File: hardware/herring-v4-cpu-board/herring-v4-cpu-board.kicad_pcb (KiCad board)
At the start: 4 copper layers, 100 x 60 mm, 18 parts, among them J1 Conn_02x20_Odd_Even, J2 Conn_02x10_Odd_Even, U1 W65C02, U2 ATF16V8B, U3 AT28C64B, U4 AS6C62256, X1 CXO_DIP8

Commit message: CPU board schematic mostly done, started routing
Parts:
- added C10: C, Capacitor_THT:C_Disc_D5.0mm_W2.5mm_P5.00mm, F.Cu at (80.2, 80.6)
- added C11: C, Capacitor_THT:C_Disc_D5.0mm_W2.5mm_P5.00mm, F.Cu at (102.7, 74.8)
- added C12: C, Capacitor_THT:C_Disc_D5.0mm_W2.5mm_P5.00mm, F.Cu at (116.8, 74.8)
- added C6: C, Capacitor_THT:C_Disc_D5.0mm_W2.5mm_P5.00mm, F.Cu at (31.8, 80.8)
- added C7: C, Capacitor_THT:C_Disc_D5.0mm_W2.5mm_P5.00mm, F.Cu at (45.7, 80.8)
- added C8: C, Capacitor_THT:C_Disc_D5.0mm_W2.5mm_P5.00mm, F.Cu at (59.7, 80.8)
- added C9: C, Capacitor_THT:C_Disc_D5.0mm_W2.5mm_P5.00mm, F.Cu at (73.7, 80.8)
- added R6: R, Resistor_THT:R_Axial_DIN0207_L6.3mm_D2.5mm_P7.62mm_Horizontal, F.Cu at (-89.1, 121.5)
- added U10: AS6C4008-55PCN, Package_DIP:DIP-32_W15.24mm, F.Cu at (75.0, 25.0)
- added U11: ATF22V10C, Package_DIP:DIP-24_W7.62mm, F.Cu at (95.0, 78.0)
- added U5: 74HC245, Package_DIP:DIP-20_W7.62mm, F.Cu at (24.0, 84.0)
- added U6: 74HC245, Package_DIP:DIP-20_W7.62mm, F.Cu at (66.0, 84.0)
- added U8: W65C22, Package_DIP:DIP-40_W15.24mm, F.Cu at (50.0, 25.0)
- added U9: SST39SF040, Package_DIP:DIP-32_W15.24mm, F.Cu at (100.0, 25.0)
- C1: value C -> C_Polarized; footprint Capacitor_THT:C_Disc_D4.3mm_W1.9mm_P5.00mm -> Capacitor_THT:CP_Radial_D10.0mm_P3.80mm
- C2, C3, C4, C5: footprint Capacitor_THT:C_Disc_D4.3mm_W1.9mm_P5.00mm -> Capacitor_THT:C_Disc_D5.0mm_W2.5mm_P5.00mm
- U2: value ATF16V8B -> 74HC245
- U3: value AT28C64B -> ATF22V10C; footprint Package_DIP:DIP-28_W15.24mm -> Package_DIP:DIP-24_W7.62mm
- U4: value AS6C62256 -> 74HC245; footprint Package_DIP:DIP-28_W15.24mm -> Package_DIP:DIP-20_W7.62mm
- moved R5 209.9 mm to (-87.5, 112.5), turned to 0 degrees
- moved R4 209.7 mm to (-87.5, 108.4), turned to 0 degrees
- moved R3 196.1 mm to (-87.5, 104.3), turned to 0 degrees
- moved R2 196.0 mm to (-87.5, 100.3), turned to 0 degrees
- moved R1 194.4 mm to (-87.5, 96.2), turned to 0 degrees
- moved C1 96.5 mm to (82.6, 103.0)
- moved X1 65.3 mm to (80.6, 92.6)
- moved C2 63.5 mm to (22.0, 42.8), turned to -90 degrees
- moved U4 53.3 mm to (52.0, 84.0), turned to 0 degrees
- moved C4 47.3 mm to (90.2, 21.8), turned to 180 degrees
- moved C5 44.1 mm to (115.2, 21.8), turned to 180 degrees
- moved J1 40.0 mm to (25.0, 115.0)
- moved J2 40.0 mm to (90.0, 115.0)
- moved G*** 33.8 mm to (74.0, 69.8)
- moved C3 33.7 mm to (47.0, 73.2), turned to 90 degrees
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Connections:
- net //RES renamed /RES
- J1 pad 10: /D5 -> D5
- J1 pad 11: /D6 -> D6
- J1 pad 12: /D7 -> D7
- J1 pad 13: /A0 -> A0
- J1 pad 14: /A1 -> A1
- J1 pad 15: /A2 -> A2
- J1 pad 16: /A3 -> A3
- J1 pad 17: /A4 -> A4
- J1 pad 18: /A5 -> A5
- J1 pad 19: /A6 -> A6
- J1 pad 20: /A7 -> A7
- J1 pad 23: /A8 -> A8
- J1 pad 24: /A9 -> A9
- J1 pad 25: /A10 -> A10
- J1 pad 26: /A11 -> A11
- J1 pad 27: /A12 -> A12
- J1 pad 28: /A13 -> A13
- J1 pad 29: /A14 -> A14
- J1 pad 30: /A15 -> A15
- J1 pad 31: /CLK -> CLK
- J1 pad 32: //CS_IO -> /IRQEXP
- J1 pad 33: //RW -> /RW
- J1 pad 34: //WR -> /NMI
- J1 pad 35: //IRQ -> BE
- J1 pad 36: //NMI -> RDY
- J1 pad 5: /D0 -> D0
- J1 pad 6: /D1 -> D1
- J1 pad 7: /D2 -> D2
- J1 pad 8: /D3 -> D3
- J1 pad 9: /D4 -> D4
- J2 pad 10: unconnected-(J2-Pad10) -> SPI_CLK
- J2 pad 11: unconnected-(J2-Pad11) -> SPI_DI
- J2 pad 12: unconnected-(J2-Pad12) -> SPI_DO
- J2 pad 13: unconnected-(J2-Pad13) -> SPI_CS0
- J2 pad 14: unconnected-(J2-Pad14) -> SPI_CS1
- J2 pad 15: unconnected-(J2-Pad15) -> SPI_CS2
- J2 pad 16: unconnected-(J2-Pad16) -> SPI_CS3
- J2 pad 17: unconnected-(J2-Pad17) -> SPI_INT0
- J2 pad 18: unconnected-(J2-Pad18) -> SPI_INT1
- J2 pad 3: //ML -> /CS0
- J2 pad 4: /RDY -> /CS1
- J2 pad 5: /BE -> /CS2
- J2 pad 6: /SYNC -> /CS3
- J2 pad 7: //VP -> /CS4
- J2 pad 8: unconnected-(J2-Pad8) -> /CS5
- J2 pad 9: unconnected-(J2-Pad9) -> /CS6
- R2 pad 2: //NMI -> /NMI
- R3 pad 2: //IRQ -> /IRQ
- R4 pad 2: /BE -> BE
- R5 pad 2: /RDY -> Net-(U1-~{SO})
- U1 pad 1: //VP -> unconnected-(U1-~{VP}-Pad1)
- U1 pad 10: /A1 -> A1CPU
- U1 pad 11: /A2 -> A2CPU
- U1 pad 12: /A3 -> A3CPU
- U1 pad 13: /A4 -> A4CPU
- U1 pad 14: /A5 -> A5CPU
- U1 pad 15: /A6 -> A6CPU
- U1 pad 16: /A7 -> A7CPU
- U1 pad 17: /A8 -> A8CPU
- U1 pad 18: /A9 -> A9CPU
- U1 pad 19: /A10 -> A10CPU
- U1 pad 2: /RDY -> RDY
- U1 pad 20: /A11 -> A11CPU
- U1 pad 22: /A12 -> A12CPU
- U1 pad 23: /A13 -> A13CPU
- U1 pad 24: /A14 -> A14CPU
- U1 pad 25: /A15 -> A15CPU
- U1 pad 26: /D7 -> D7CPU
- U1 pad 27: /D6 -> D6CPU
- U1 pad 28: /D5 -> D5CPU
- U1 pad 29: /D4 -> D4CPU
- U1 pad 30: /D3 -> D3CPU
- U1 pad 31: /D2 -> D2CPU
- U1 pad 32: /D1 -> D1CPU
- U1 pad 33: /D0 -> D0CPU
- U1 pad 34: //RW -> /RWCPU
- U1 pad 36: /BE -> BE
- U1 pad 37: /CLK -> CLKCPU
- U1 pad 38: +5V -> Net-(U1-~{SO})
- U1 pad 4: //IRQ -> /IRQ
- U1 pad 5: //ML -> unconnected-(U1-~{ML}-Pad5)
- U1 pad 6: //NMI -> /NMI
- U1 pad 7: /SYNC -> unconnected-(U1-SYNC-Pad7)
- U1 pad 9: /A0 -> A0CPU
- U2 pad 1: /CLK -> GND
- U2 pad 11: //RW -> A0CPU
- U2 pad 12: //ROM0 -> A1CPU
- U2 pad 13: //RAM0 -> A2CPU
- U2 pad 14: //CS_IO -> A3CPU
- U2 pad 15: //WR -> A4CPU
- U2 pad 16: unconnected-(U2-Pad16) -> A5CPU
- U2 pad 17: unconnected-(U2-Pad17) -> A6CPU
- U2 pad 18: unconnected-(U2-Pad18) -> A7CPU
- U2 pad 19: unconnected-(U2-Pad19) -> /BUFFERS
- U2 pad 2: /A8 -> A7
- U2 pad 3: /A9 -> A6
- U2 pad 4: /A10 -> A5
- U2 pad 5: /A11 -> A4
- U2 pad 6: /A12 -> A3
- U2 pad 7: /A13 -> A2
- U2 pad 8: /A14 -> A1
- U2 pad 9: /A15 -> A0
- U3 pad 1: unconnected-(U3-Pad1) -> BE
- U3 pad 10: /A0 -> A14CPU
- U3 pad 11: /D0 -> A15CPU
- U3 pad 12: /D1 -> GND
- U3 pad 13: /D2 -> GND
- U3 pad 14: GND -> /BUFFERS
- U3 pad 15: /D3 -> unconnected-(U3-IO1-Pad15)
- U3 pad 16: /D4 -> /CSVIA
- U3 pad 17: /D5 -> /CS6
- U3 pad 18: /D6 -> /CS5
- U3 pad 19: /D7 -> /CS4
- U3 pad 2: /A12 -> A6CPU
- U3 pad 20: //ROM0 -> /CS3
- U3 pad 21: /A10 -> /CS2
- U3 pad 22: GND -> /CS1
- U3 pad 23: /A11 -> /CS0
- U3 pad 24: /A9 -> +5V
- U3 pad 3: /A7 -> A7CPU
- U3 pad 4: /A6 -> A8CPU
- U3 pad 5: /A5 -> A9CPU
- U3 pad 6: /A4 -> A10CPU
- U3 pad 7: /A3 -> A11CPU
- U3 pad 8: /A2 -> A12CPU
- U3 pad 9: /A1 -> A13CPU
- U4 pad 1: /A14 -> GND
- U4 pad 10: /A0 -> GND
- U4 pad 11: /D0 -> A8CPU
- U4 pad 12: /D1 -> A9CPU
- U4 pad 13: /D2 -> A10CPU
- U4 pad 14: GND -> A11CPU
- U4 pad 15: /D3 -> A12CPU
- U4 pad 16: /D4 -> A13CPU
- U4 pad 17: /D5 -> A14CPU
- U4 pad 18: /D6 -> A15CPU
- U4 pad 19: /D7 -> /BUFFERS
- U4 pad 2: /A12 -> A15
- U4 pad 20: //RAM0 -> +5V
- U4 pad 3: /A7 -> A14
- U4 pad 4: /A6 -> A13
- U4 pad 5: /A5 -> A12
- U4 pad 6: /A4 -> A11
- U4 pad 7: /A3 -> A10
- U4 pad 8: /A2 -> A9
- U4 pad 9: /A1 -> A8
- X1 pad 5: /CLK -> CLKCPU
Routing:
- net /D1: track 162.1 -> 0.00 mm, vias 1 -> 0
- net /D2: track 159.3 -> 0.00 mm, vias 1 -> 0
- net /D0: track 158.5 -> 0.00 mm, vias 1 -> 0
- net /D3: track 155.2 -> 0.00 mm, vias 1 -> 0
- net /D5: track 147.3 -> 0.00 mm, vias 1 -> 0
- net /D4: track 147.2 -> 0.00 mm, vias 1 -> 0
- net /D6: track 138.5 -> 0.00 mm, vias 1 -> 0
- net /D7: track 137.2 -> 0.00 mm, vias 1 -> 0
- net /RES: track 130.3 -> 0.00 mm, vias 2 -> 0
- net /RDY: track 126.6 -> 0.00 mm, vias 2 -> 0
- net /A0: track 121.8 -> 0.00 mm, vias 1 -> 0
- net //IRQ: track 121.4 -> 0.00 mm, vias 4 -> 0
- net /BE: track 121.2 -> 0.00 mm, vias 2 -> 0
- net /A1: track 119.2 -> 0.00 mm, vias 1 -> 0
- net /A2: track 111.2 -> 0.00 mm, vias 1 -> 0
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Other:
- board size 100 x 60 mm -> 100 x 100 mm
- board text added: "Herring v4 CPU Board Rev 1.0a github.com/crmaykish/herring-6502"
- board text removed: "32K SRAM"
- board text removed: "65C02"
- board text removed: "8K ROM"
- board text removed: "CLOCK"
- board text removed: "GAL16V8"
- board text removed: "Herring v4 Core Board Rev 1.0a Colin Maykish - 2024"
- board text removed: "JLCJLCJLCJLC"
- board text removed: "github.com/crmaykish/herring-6502"

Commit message: Routed buffers and expansion header
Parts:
- removed C1: C_Polarized, Capacitor_THT:CP_Radial_D10.0mm_P3.80mm
- removed C10, C11, C12: C, Capacitor_THT:C_Disc_D5.0mm_W2.5mm_P5.00mm
- removed the C4 at (90.2, 21.8)
- removed the C5 at (115.2, 21.8)
- removed the C6 at (31.8, 80.8)
- removed R1, R2, R3, R4, R5, R6: R, Resistor_THT:R_Axial_DIN0207_L6.3mm_D2.5mm_P7.62mm_Horizontal
- removed U1: W65C02, Package_DIP:DIP-40_W15.24mm
- removed U10: AS6C4008-55PCN, Package_DIP:DIP-32_W15.24mm
- removed U11: ATF22V10C, Package_DIP:DIP-24_W7.62mm
- removed the U3 at (109.0, 78.0)
- removed the U8 at (50.0, 25.0)
- removed U9: SST39SF040, Package_DIP:DIP-32_W15.24mm
- removed X1: CXO_DIP8, Oscillator:Oscillator_DIP-8
- added U2: ATF22V10C, Package_DIP:DIP-24_W7.62mm, F.Cu at (80.0, 78.9)
- moved G*** 105.2 mm to (178.5, 81.6)
- moved C3 44.5 mm to (45.7, 80.4), turned to 180 degrees
- moved C5 27.6 mm to (73.8, 80.0), turned to 180 degrees
- moved C6 14.9 mm to (87.3, 74.8)
- moved C2 14.0 mm to (31.7, 80.0)
- renumbered C7 to C2, C2 to C3, C8 to C4, C3 to C5, C9 to C6, U2 to U3, U5 to U6, U6 to U8
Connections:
- J1 pad 10: D5 -> BD5
- J1 pad 11: D6 -> BD6
- J1 pad 12: D7 -> BD7
- J1 pad 13: A0 -> BA0
- J1 pad 14: A1 -> BA1
- J1 pad 15: A2 -> BA2
- J1 pad 16: A3 -> BA3
- J1 pad 17: A4 -> BA4
- J1 pad 18: A5 -> BA5
- J1 pad 19: A6 -> BA6
- J1 pad 20: A7 -> BA7
- J1 pad 23: A8 -> BA8
- J1 pad 24: A9 -> BA9
- J1 pad 25: A10 -> BA10
- J1 pad 26: A11 -> BA11
- J1 pad 27: A12 -> BA12
- J1 pad 28: A13 -> BA13
- J1 pad 29: A14 -> BA14
- J1 pad 30: A15 -> BA15
- J1 pad 31: CLK -> BCLKCPU
- J1 pad 32: /IRQEXP -> /BRW
- J1 pad 33: /RW -> BE
- J1 pad 34: /NMI -> /MEMWR
- J1 pad 35: BE -> /IOREQ
- J1 pad 36: RDY -> /MEMRQ
- J1 pad 5: D0 -> BD0
- J1 pad 6: D1 -> BD1
- J1 pad 7: D2 -> BD2
- J1 pad 8: D3 -> BD3
- J1 pad 9: D4 -> BD4
- J2 pad 3: /CS0 -> /IRQ0
- J2 pad 4: /CS1 -> /IRQ1
- J2 pad 5: /CS2 -> /IRQ2
- J2 pad 6: /CS3 -> /IRQ3
- J2 pad 7: /CS4 -> /NMI
- J2 pad 8: /CS5 -> /BVP
- J2 pad 9: /CS6 -> RDY
- U3 pad 11: A0CPU -> A0
- U3 pad 12: A1CPU -> A1
- U3 pad 13: A2CPU -> A2
- U3 pad 14: A3CPU -> A3
- U3 pad 15: A4CPU -> A4
- U3 pad 16: A5CPU -> A5
- U3 pad 17: A6CPU -> A6
- U3 pad 18: A7CPU -> A7
- U3 pad 2: A7 -> BA7
- U3 pad 3: A6 -> BA6
- U3 pad 4: A5 -> BA5
- U3 pad 5: A4 -> BA4
- U3 pad 6: A3 -> BA3
- U3 pad 7: A2 -> BA2
- U3 pad 8: A1 -> BA1
- U3 pad 9: A0 -> BA0
- U4 pad 11: A8CPU -> A8
- U4 pad 12: A9CPU -> A9
- U4 pad 13: A10CPU -> A10
- U4 pad 14: A11CPU -> A11
- U4 pad 15: A12CPU -> A12
- U4 pad 16: A13CPU -> A13
- U4 pad 17: A14CPU -> A14
- U4 pad 18: A15CPU -> A15
- U4 pad 2: A15 -> BA15
- U4 pad 3: A14 -> BA14
- U4 pad 4: A13 -> BA13
- U4 pad 5: A12 -> BA12
- U4 pad 6: A11 -> BA11
- U4 pad 7: A10 -> BA10
- U4 pad 8: A9 -> BA9
- U4 pad 9: A8 -> BA8
- U6 pad 1: /RWCPU -> /RW
- U6 pad 11: D0CPU -> D0
- U6 pad 12: D1CPU -> D1
- U6 pad 13: D2CPU -> D2
- U6 pad 14: D3CPU -> D3
- U6 pad 15: D4CPU -> D4
- U6 pad 16: D5CPU -> D5
- U6 pad 17: D6CPU -> D6
- U6 pad 18: D7CPU -> D7
- U6 pad 2: D7 -> BD7
- U6 pad 3: D6 -> BD6
- U6 pad 4: D5 -> BD5
- U6 pad 5: D4 -> BD4
- U6 pad 6: D3 -> BD3
- U6 pad 7: D2 -> BD2
- U6 pad 8: D1 -> BD1
- U6 pad 9: D0 -> BD0
- U8 pad 1: +5V -> GND
- U8 pad 11: unconnected-(U6-B7-Pad11) -> GND
- U8 pad 12: unconnected-(U6-B6-Pad12) -> GND
- U8 pad 13: unconnected-(U6-B5-Pad13) -> GND
- U8 pad 14: unconnected-(U6-B4-Pad14) -> GND
- U8 pad 15: unconnected-(U6-B3-Pad15) -> GND
- U8 pad 16: unconnected-(U6-B2-Pad16) -> CLKCPU
- U8 pad 18: CLK -> /VP
- U8 pad 2: CLKCPU -> /BVP
- U8 pad 3: /RWCPU -> /BRW
- U8 pad 4: GND -> BCLKCPU
- U8 pad 5: GND -> unconnected-(U8-A3-Pad5)
- U8 pad 6: GND -> unconnected-(U8-A4-Pad6)
- U8 pad 7: GND -> unconnected-(U8-A5-Pad7)
- U8 pad 8: GND -> unconnected-(U8-A6-Pad8)
- U8 pad 9: GND -> unconnected-(U8-A7-Pad9)
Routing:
- net /BUFFERS: track 0.00 -> 79.1 mm, vias 0 -> 4
- net /RW: track 0.00 -> 67.6 mm, vias 0 -> 1
- net /BVP: track 0.00 -> 62.4 mm, vias 0 -> 2
- net /MEMWR: track 0.00 -> 48.8 mm, vias 0 -> 2
- net BE: track 0.00 -> 47.5 mm, vias 0 -> 2
- net /MEMRQ: track 0.00 -> 43.1 mm, vias 0 -> 2
- net /IOREQ: track 0.00 -> 42.9 mm, vias 0 -> 2
- net D7: track 39.0 -> 0.00 mm
- net BD7: track 0.00 -> 39.0 mm
- net BA7: track 0.00 -> 36.4 mm
- net A7: track 36.4 -> 0.00 mm
- net BA15: track 0.00 -> 35.6 mm
- net D6: track 32.8 -> 0.00 mm
- net BD6: track 0.00 -> 32.8 mm
- net D5: track 32.5 -> 0.00 mm
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
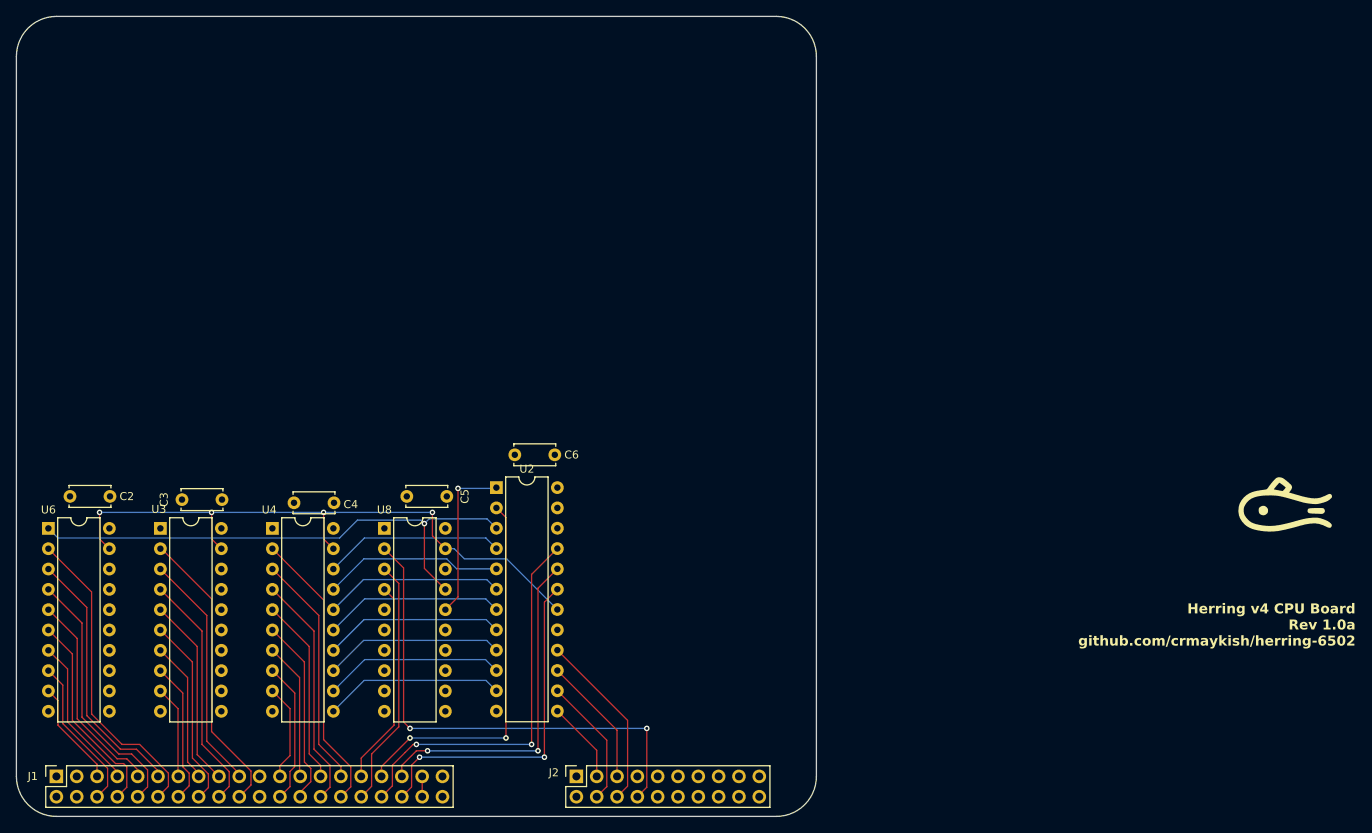
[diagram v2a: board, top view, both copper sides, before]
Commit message: v4 CPU board fully routed, needs cleanup
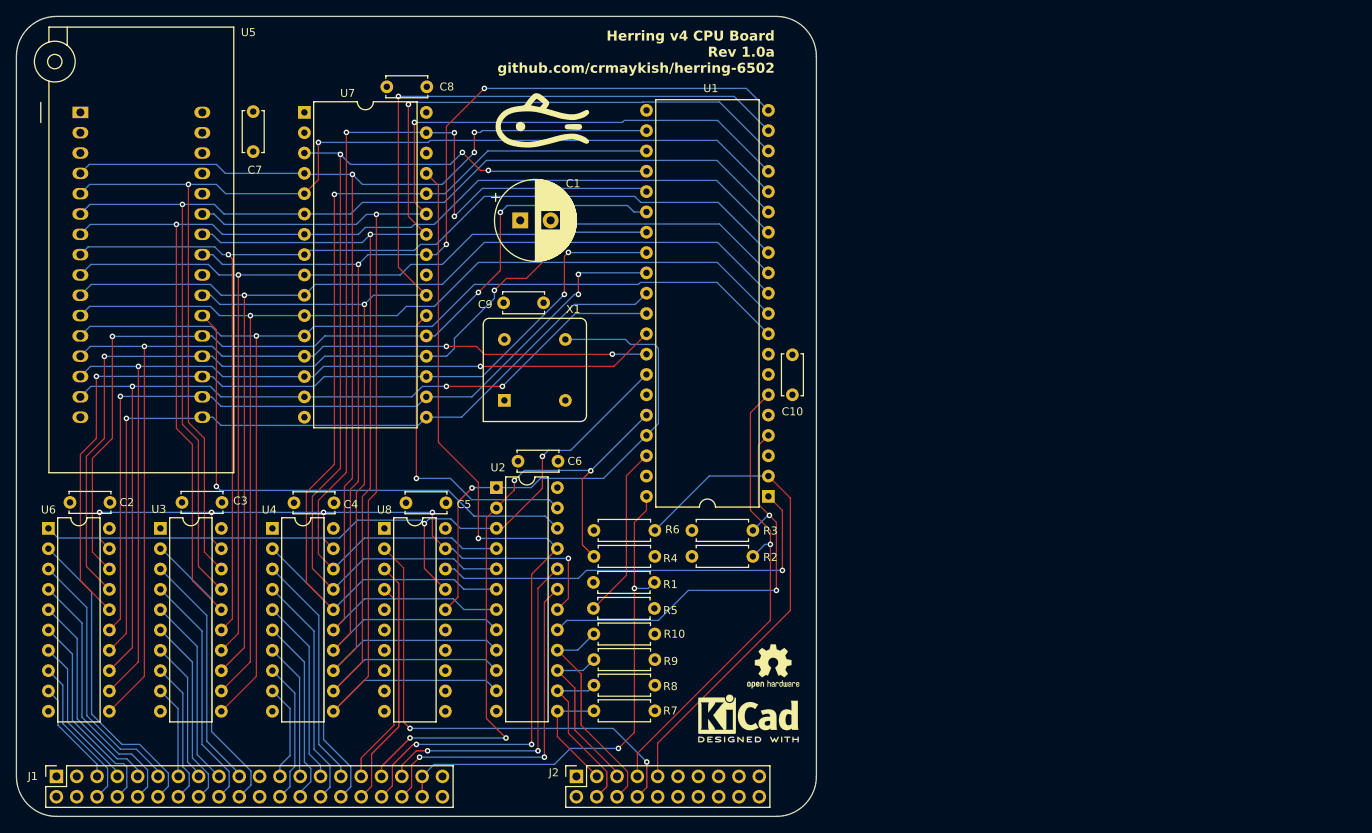
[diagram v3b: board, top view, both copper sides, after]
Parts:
- added C1: C_Polarized, Capacitor_THT:CP_Radial_D10.0mm_P3.80mm, F.Cu at (83.0, 45.5)
- added C10: C, Capacitor_THT:C_Disc_D5.0mm_W2.5mm_P5.00mm, F.Cu at (117.0, 62.3)
- added C7: C, Capacitor_THT:C_Disc_D5.0mm_W2.5mm_P5.00mm, F.Cu at (49.6, 31.9)
- added C8: C, Capacitor_THT:C_Disc_D5.0mm_W2.5mm_P5.00mm, F.Cu at (71.3, 28.8)
- added C9: C, Capacitor_THT:C_Disc_D5.0mm_W2.5mm_P5.00mm, F.Cu at (80.9, 55.8)
- added R1: R, Resistor_THT:R_Axial_DIN0207_L6.3mm_D2.5mm_P7.62mm_Horizontal, F.Cu at (92.1, 90.8)
- added R10: R, Resistor_THT:R_Axial_DIN0207_L6.3mm_D2.5mm_P7.62mm_Horizontal, F.Cu at (92.2, 97.2)
- added R2: R, Resistor_THT:R_Axial_DIN0207_L6.3mm_D2.5mm_P7.62mm_Horizontal, F.Cu at (104.4, 87.5)
- added R3: R, Resistor_THT:R_Axial_DIN0207_L6.3mm_D2.5mm_P7.62mm_Horizontal, F.Cu at (104.4, 84.2)
- added R4: R, Resistor_THT:R_Axial_DIN0207_L6.3mm_D2.5mm_P7.62mm_Horizontal, F.Cu at (99.8, 87.5)
- added R5: R, Resistor_THT:R_Axial_DIN0207_L6.3mm_D2.5mm_P7.62mm_Horizontal, F.Cu at (99.8, 94.0)
- added R6: R, Resistor_THT:R_Axial_DIN0207_L6.3mm_D2.5mm_P7.62mm_Horizontal, F.Cu at (92.2, 84.2)
- added R7: R, Resistor_THT:R_Axial_DIN0207_L6.3mm_D2.5mm_P7.62mm_Horizontal, F.Cu at (92.2, 106.8)
- added R8: R, Resistor_THT:R_Axial_DIN0207_L6.3mm_D2.5mm_P7.62mm_Horizontal, F.Cu at (92.2, 103.6)
- added R9: R, Resistor_THT:R_Axial_DIN0207_L6.3mm_D2.5mm_P7.62mm_Horizontal, F.Cu at (92.2, 100.4)
- added REF**: KiCad-Logo2_5mm_SilkScreen, Symbol:KiCad-Logo2_5mm_SilkScreen, F.Cu at (111.5, 107.8)
- added REF**: OSHW-Logo2_7.3x6mm_SilkScreen, Symbol:OSHW-Logo2_7.3x6mm_SilkScreen, F.Cu at (114.6, 101.2)
- added U1: W65C02, Package_DIP:DIP-40_W15.24mm, F.Cu at (114.0, 80.0)
- added U5: SST39SF040, Socket:DIP_Socket-32_W11.9_W12.7_W15.24_W17.78_W18.5_3M_232-1285-00-0602J, F.Cu at (28.0, 32.0)
- added U7: AS6C4008-55PCN, Package_DIP:DIP-32_W15.24mm, F.Cu at (56.0, 32.0)
- added X1: CXO_DIP8, Oscillator:Oscillator_DIP-8, F.Cu at (81.0, 68.0)
- moved G*** 104.5 mm to (85.7, 33.6)
- moved C6 0.89 mm to (87.7, 75.6)
- moved C5 0.81 mm to (73.7, 80.8)
- moved C2 0.75 mm to (31.7, 80.8)
- moved C3 0.35 mm to (45.7, 80.8)
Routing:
- net A9: track 22.6 -> 175.2 mm, vias 0 -> 2
- net A8: track 22.5 -> 175.0 mm, vias 0 -> 2
- net A10: track 22.5 -> 173.1 mm, vias 0 -> 2
- net A7: track 0.00 -> 144.9 mm, vias 0 -> 2
- net A5: track 0.00 -> 143.0 mm, vias 0 -> 1
- net A6: track 0.00 -> 142.6 mm, vias 0 -> 1
- net A0: track 0.00 -> 141.2 mm, vias 0 -> 1
- net A1: track 0.00 -> 140.8 mm, vias 0 -> 1
- net A2: track 0.00 -> 140.6 mm, vias 0 -> 1
- net A4: track 0.00 -> 140.4 mm, vias 0 -> 1
- net A3: track 0.00 -> 140.1 mm, vias 0 -> 1
- net A11: track 22.5 -> 162.2 mm, vias 0 -> 3
- net A12: track 22.6 -> 157.0 mm, vias 0 -> 3
- net D0: track 0.00 -> 120.1 mm, vias 0 -> 3
- net D1: track 0.00 -> 116.1 mm, vias 0 -> 2
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
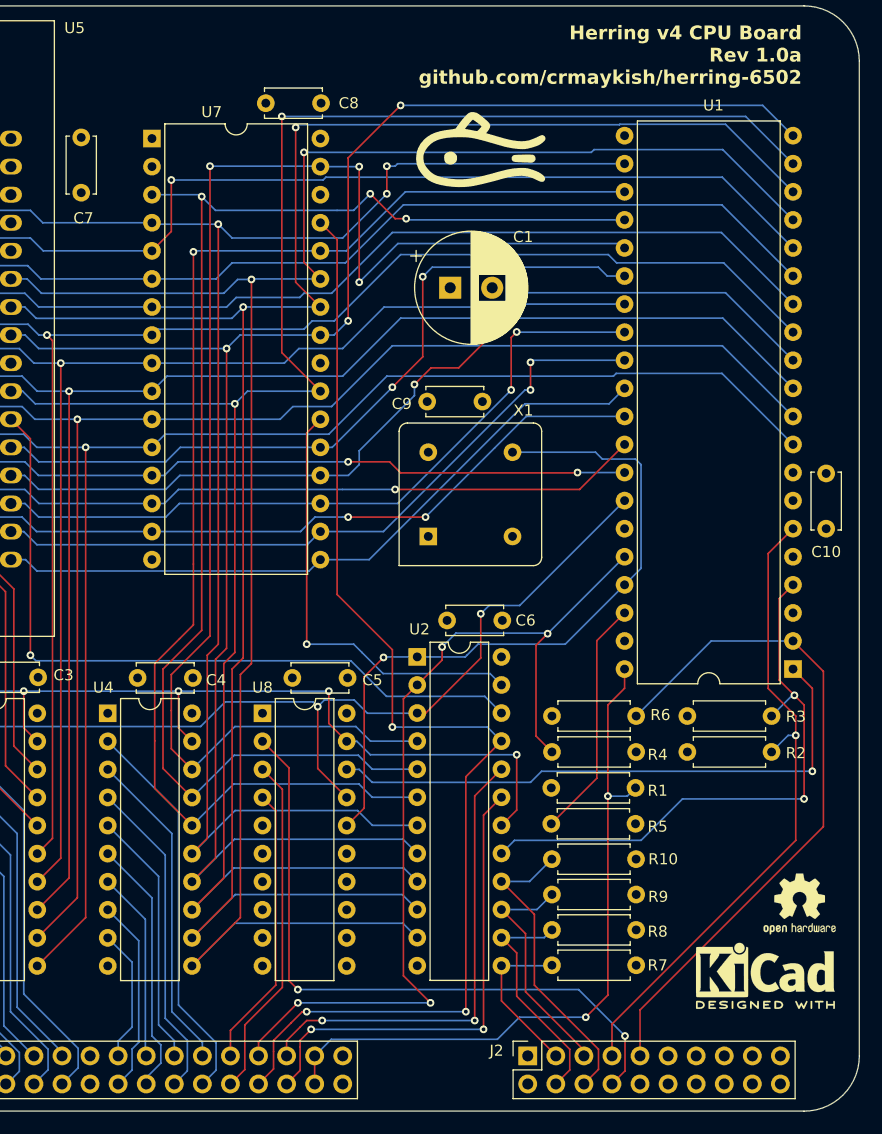
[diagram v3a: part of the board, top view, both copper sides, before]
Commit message: Stub out v4 ACIA board
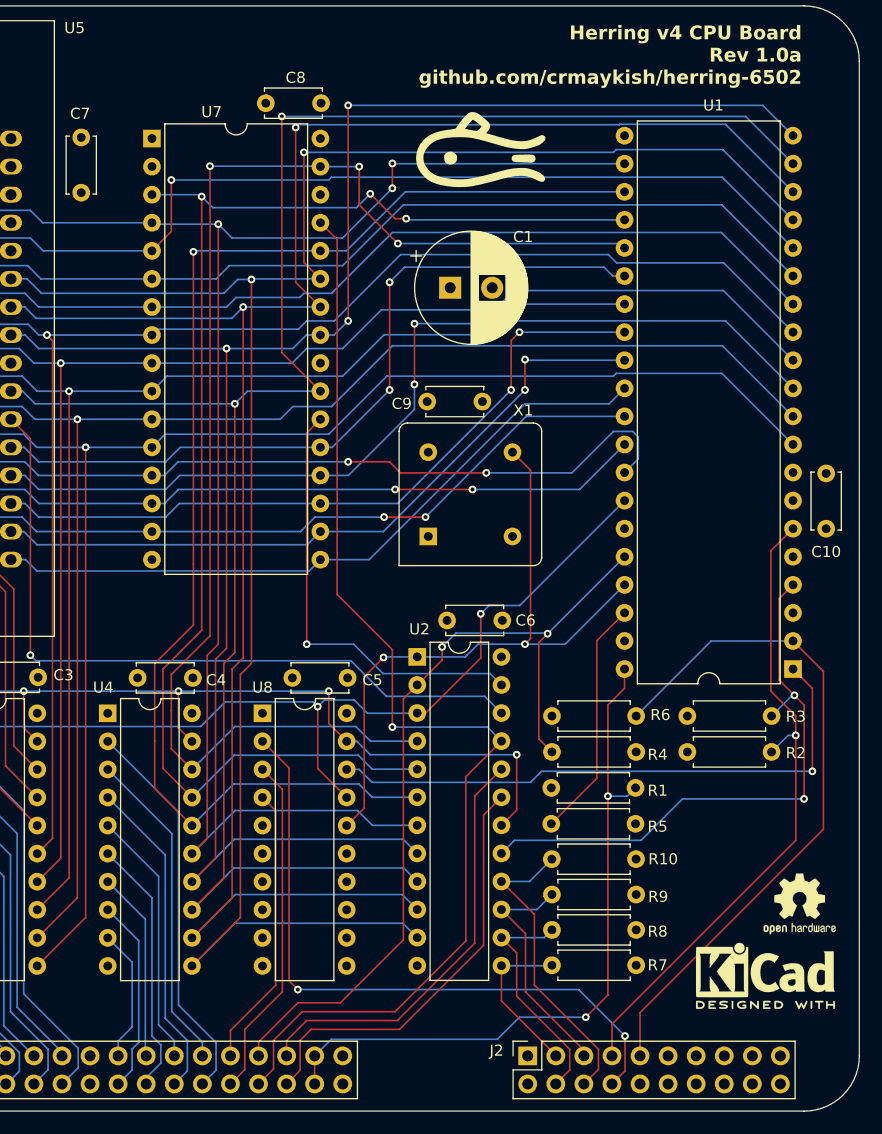
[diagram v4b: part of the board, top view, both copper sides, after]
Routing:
- net BE: track 84.6 -> 77.6 mm, vias 4 -> 2
- net A15: track 128.9 -> 121.9 mm
- net D0: track 120.1 -> 126.9 mm
- net CLKCPU: track 64.7 -> 59.4 mm, vias 1 -> 2
- net /MEMRQ: track 43.1 -> 38.7 mm, vias 2 -> 0
- net /IOREQ: track 42.9 -> 38.8 mm, vias 2 -> 0
- net /MEMWR: track 107.5 -> 103.8 mm, vias 3 -> 1
- net D6: track 107.8 -> 111.0 mm
- net A11: track 162.2 -> 165.0 mm
- net D7: track 110.2 -> 111.7 mm
- net D1: vias 2 -> 3
